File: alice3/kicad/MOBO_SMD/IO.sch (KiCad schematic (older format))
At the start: 36 parts, among them CON1 MicroSD, P2 USB_OTG, P3 UART1, SW2 SOFT RESET, U5 STM32F415RG, X1 MINI_DIN_6, Y2 16MHz

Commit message: Assign parts to footprints.
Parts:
- F1: footprint (none) -> Resistors_SMD:R_1210
- R22, R23, R24, R25: footprint (none) -> Resistors_SMD:R_0805
- X1: footprint mini_din-M_DIN6 -> cui-md-xxs:cui-md-60s
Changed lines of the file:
@@
 $EndDescr
 $Comp
-L +3.3V #PWR32
+L +3.3V #PWR014
 U 1 1 5689970E
 P 5750 950
-F 0 "#PWR32" H 5750 800 50  0001 C CNN
+F 0 "#PWR014" H 5750 800 50  0001 C CNN
 F 1 "+3.3V" H 5750 1090 50  0000 C CNN
 F 2 "" H 5750 950 60  0000 C CNN
@@
 NoConn ~ 8050 4700
 $Comp
-L GND #PWR35
+L GND #PWR015
 U 1 1 56899C9B
 P 7150 5900
-F 0 "#PWR35" H 7150 5650 50  0001 C CNN
+F 0 "#PWR015" H 7150 5650 50  0001 C CNN
 F 1 "GND" H 7150 5750 50  0000 C CNN
 F 2 "" H 7150 5900 60  0000 C CNN
@@
 $EndComp
 $Comp
-L +3.3V #PWR34
+L +3.3V #PWR016
 U 1 1 56899CD4
 P 7050 4050
-F 0 "#PWR34" H 7050 3900 50  0001 C CNN
+F 0 "#PWR016" H 7050 3900 50  0001 C CNN
 F 1 "+3.3V" H 7050 4190 50  0000 C CNN
 F 2 "" H 7050 4050 60  0000 C CNN
@@
 $EndComp
 $Comp
-L GND #PWR33
+L GND #PWR017
 U 1 1 568A1142
 P 5750 2250
-F 0 "#PWR33" H 5750 2000 50  0001 C CNN
+F 0 "#PWR017" H 5750 2000 50  0001 C CNN
 F 1 "GND" H 5750 2100 50  0000 C CNN
 F 2 "" H 5750 2250 60  0000 C CNN
@@
 NoConn ~ 8050 5400
 $Comp
-L PWR_FLAG #FLG1
+L PWR_FLAG #FLG018
 U 1 1 56A07E43
 P 8300 1300
-F 0 "#FLG1" H 8300 1395 50  0001 C CNN
+F 0 "#FLG018" H 8300 1395 50  0001 C CNN
 F 1 "PWR_FLAG" H 8300 1480 50  0000 C CNN
 F 2 "" H 8300 1300 50  0000 C CNN
@@
 $EndComp
 $Comp
-L +5V #PWR38
+L +5V #PWR019
 U 1 1 56A07E73
 P 8300 1600
-F 0 "#PWR38" H 8300 1450 50  0001 C CNN
+F 0 "#PWR019" H 8300 1450 50  0001 C CNN
 F 1 "+5V" H 8300 1740 50  0000 C CNN
 F 2 "" H 8300 1600 50  0000 C CNN
@@
 $EndComp
 $Comp
-L PWR_FLAG #FLG2
+L PWR_FLAG #FLG020
 U 1 1 56A0800D
 P 8900 1300
-F 0 "#FLG2" H 8900 1395 50  0001 C CNN
+F 0 "#FLG020" H 8900 1395 50  0001 C CNN
 F 1 "PWR_FLAG" H 8900 1480 50  0000 C CNN
 F 2 "" H 8900 1300 50  0000 C CNN
@@
 $EndComp
 $Comp
-L GND #PWR39
+L GND #PWR021
 U 1 1 56A08038
 P 8900 1600
-F 0 "#PWR39" H 8900 1350 50  0001 C CNN
+F 0 "#PWR021" H 8900 1350 50  0001 C CNN
 F 1 "GND" H 8900 1450 50  0000 C CNN
 F 2 "" H 8900 1600 50  0000 C CNN
@@
 $EndComp
 $Comp
-L GND #PWR37
+L GND #PWR022
 U 1 1 56A0883B
 P 7950 3100
-F 0 "#PWR37" H 7950 2850 50  0001 C CNN
+F 0 "#PWR022" H 7950 2850 50  0001 C CNN
 F 1 "GND" H 7950 2950 50  0000 C CNN
 F 2 "" H 7950 3100 50  0000 C CNN
@@
 $EndComp
 $Comp
-L +3.3V #PWR36
+L +3.3V #PWR023
 U 1 1 56A08841
 P 7500 2350
-F 0 "#PWR36" H 7500 2200 50  0001 C CNN
+F 0 "#PWR023" H 7500 2200 50  0001 C CNN
 F 1 "+3.3V" H 7500 2490 50  0000 C CNN
 F 2 "" H 7500 2350 50  0000 C CNN
@@
 A0
 $Comp
-L GND #PWR22
+L GND #PWR024
 U 1 1 56B85293
 P 1700 2800
-F 0 "#PWR22" H 1700 2550 50  0001 C CNN
+F 0 "#PWR024" H 1700 2550 50  0001 C CNN
 F 1 "GND" H 1700 2650 50  0000 C CNN
 F 2 "" H 1700 2800 60  0000 C CNN
@@
 $EndComp
 $Comp
-L +3.3V #PWR27
+L +3.3V #PWR025
 U 1 1 56BA49D2
 P 2300 1300
-F 0 "#PWR27" H 2300 1150 50  0001 C CNN
+F 0 "#PWR025" H 2300 1150 50  0001 C CNN
 F 1 "+3.3V" H 2300 1440 50  0000 C CNN
 F 2 "" H 2300 1300 60  0000 C CNN
@@
 $EndComp
 $Comp
-L GND #PWR23
+L GND #PWR026
 U 1 1 56BA4C6B
 P 1800 1400
-F 0 "#PWR23" H 1800 1150 50  0001 C CNN
+F 0 "#PWR026" H 1800 1150 50  0001 C CNN
 F 1 "GND" H 1800 1250 50  0000 C CNN
 F 2 "" H 1800 1400 60  0000 C CNN
@@
 $EndComp
 $Comp
-L GND #PWR31
+L GND #PWR027
 U 1 1 56BA634D
 P 4800 1450
-F 0 "#PWR31" H 4800 1200 50  0001 C CNN
+F 0 "#PWR027" H 4800 1200 50  0001 C CNN
 F 1 "GND" H 4800 1300 50  0000 C CNN
 F 2 "" H 4800 1450 60  0000 C CNN
@@
 $EndComp
 $Comp
-L +3.3V #PWR15
+L +3.3V #PWR028
 U 1 1 56BA6501
 P 900 2600
-F 0 "#PWR15" H 900 2450 50  0001 C CNN
+F 0 "#PWR028" H 900 2450 50  0001 C CNN
 F 1 "+3.3V" H 900 2740 50  0000 C CNN
 F 2 "" H 900 2600 60  0000 C CNN
@@
 $EndComp
 $Comp
-L GND #PWR16
+L GND #PWR029
 U 1 1 56BA66E5
 P 900 3450
-F 0 "#PWR16" H 900 3200 50  0001 C CNN
+F 0 "#PWR029" H 900 3200 50  0001 C CNN
 F 1 "GND" H 900 3300 50  0000 C CNN
 F 2 "" H 900 3450 60  0000 C CNN
@@
 $EndComp
 $Comp
-L +3.3V #PWR17
+L +3.3V #PWR030
 U 1 1 56BA9EA1
 P 1000 1900
-F 0 "#PWR17" H 1000 1750 50  0001 C CNN
+F 0 "#PWR030" H 1000 1750 50  0001 C CNN
 F 1 "+3.3V" H 1000 2040 50  0000 C CNN
 F 2 "" H 1000 1900 60  0000 C CNN
@@
 $EndComp
 $Comp
-L GND #PWR21
+L GND #PWR031
 U 1 1 56BAAE8C
 P 1600 2500
-F 0 "#PWR21" H 1600 2250 50  0001 C CNN
+F 0 "#PWR031" H 1600 2250 50  0001 C CNN
 F 1 "GND" H 1600 2350 50  0000 C CNN
 F 2 "" H 1600 2500 60  0000 C CNN
@@
 $EndComp
 $Comp
-L GND #PWR20
+L GND #PWR032
 U 1 1 56BAAEE8
 P 1450 2400
-F 0 "#PWR20" H 1450 2150 50  0001 C CNN
+F 0 "#PWR032" H 1450 2150 50  0001 C CNN
 F 1 "GND" H 1450 2250 50  0000 C CNN
 F 2 "" H 1450 2400 60  0000 C CNN
@@
 $EndComp
 $Comp
-L GND #PWR19
+L GND #PWR033
 U 1 1 56BAAF44
 P 1300 2300
-F 0 "#PWR19" H 1300 2050 50  0001 C CNN
+F 0 "#PWR033" H 1300 2050 50  0001 C CNN
 F 1 "GND" H 1300 2150 50  0000 C CNN
 F 2 "" H 1300 2300 60  0000 C CNN
@@
 $EndComp
 $Comp
-L GND #PWR18
+L GND #PWR034
 U 1 1 56BAAFA0
 P 1150 2200
-F 0 "#PWR18" H 1150 1950 50  0001 C CNN
+F 0 "#PWR034" H 1150 1950 50  0001 C CNN
 F 1 "GND" H 1150 2050 50  0000 C CNN
 F 2 "" H 1150 2200 60  0000 C CNN
@@
 $EndComp
 $Comp
-L GND #PWR14
+L GND #PWR035
 U 1 1 56BAAFFC
 P 800 2150
-F 0 "#PWR14" H 800 1900 50  0001 C CNN
+F 0 "#PWR035" H 800 1900 50  0001 C CNN
 F 1 "GND" H 800 2000 50  0000 C CNN
 F 2 "" H 800 2150 60  0000 C CNN
@@
 USB_D_P
 $Comp
-L GND #PWR24
+L GND #PWR036
 U 1 1 56BAB684
 P 1800 5850
-F 0 "#PWR24" H 1800 5600 50  0001 C CNN
+F 0 "#PWR036" H 1800 5600 50  0001 C CNN
 F 1 "GND" H 1800 5700 50  0000 C CNN
 F 2 "" H 1800 5850 60  0000 C CNN
@@
 $EndComp
 $Comp
-L +5V #PWR26
+L +5V #PWR037
 U 1 1 56BABB53
 P 2150 6990
-F 0 "#PWR26" H 2150 6840 50  0001 C CNN
+F 0 "#PWR037" H 2150 6840 50  0001 C CNN
 F 1 "+5V" H 2150 7130 50  0000 C CNN
 F 2 "" H 2150 6990 60  0000 C CNN
@@
 $EndComp
 $Comp
-L GND #PWR25
+L GND #PWR038
 U 1 1 56BAC7E3
 P 1850 7260
-F 0 "#PWR25" H 1850 7010 50  0001 C CNN
+F 0 "#PWR038" H 1850 7010 50  0001 C CNN
 F 1 "GND" H 1850 7110 50  0000 C CNN
 F 2 "" H 1850 7260 60  0000 C CNN
@@
 F 0 "X1" H 3400 7075 50  0000 L BNN
 F 1 "MINI_DIN_6" H 3800 7075 50  0000 L BNN
-F 2 "mini_din-M_DIN6" H 3800 6700 50  0001 C CNN
+F 2 "cui-md-xxs:cui-md-60s" H 3800 6700 50  0001 C CNN
 F 3 "" H 3800 6550 60  0000 C CNN
 	1    3800 6550
@@
 	1850 7220 1850 7260
 $Comp
-L +5V #PWR28
+L +5V #PWR039
 U 1 1 56CE0CE0
 P 3125 6200
-F 0 "#PWR28" H 3125 6050 50  0001 C CNN
+F 0 "#PWR039" H 3125 6050 50  0001 C CNN
 F 1 "+5V" H 3125 6340 50  0000 C CNN
 F 2 "" H 3125 6200 60  0000 C CNN
@@
 F 0 "R24" V 5130 6350 50  0000 C CNN
 F 1 "100" V 5050 6350 50  0000 C CNN
-F 2 "" V 4980 6350 30  0000 C CNN
+F 2 "Resistors_SMD:R_0805" V 4980 6350 30  0001 C CNN
 F 3 "" H 5050 6350 30  0000 C CNN
 	1    5050 6350
@@
 F 0 "R25" V 5130 6650 50  0000 C CNN
 F 1 "100" V 5050 6650 50  0000 C CNN
-F 2 "" V 4980 6650 30  0000 C CNN
+F 2 "Resistors_SMD:R_0805" V 4980 6650 30  0001 C CNN
 F 3 "" H 5050 6650 30  0000 C CNN
 	1    5050 6650
@@
 F 0 "R23" V 4880 6150 50  0000 C CNN
 F 1 "10K" V 4800 6150 50  0000 C CNN
-F 2 "" V 4730 6150 30  0000 C CNN
+F 2 "Resistors_SMD:R_0805" V 4730 6150 30  0001 C CNN
 F 3 "" H 4800 6150 30  0000 C CNN
 	1    4800 6150
@@
 F 0 "R22" V 4655 6150 50  0000 C CNN
 F 1 "10K" V 4575 6150 50  0000 C CNN
-F 2 "" V 4505 6150 30  0000 C CNN
+F 2 "Resistors_SMD:R_0805" V 4505 6150 30  0001 C CNN
 F 3 "" H 4575 6150 30  0000 C CNN
 	1    4575 6150
@@
 Connection ~ 4575 6650
 $Comp
-L +5V #PWR30
+L +5V #PWR040
 U 1 1 56CE2231
 P 4575 5900
-F 0 "#PWR30" H 4575 5750 50  0001 C CNN
+F 0 "#PWR040" H 4575 5750 50  0001 C CNN
 F 1 "+5V" H 4575 6040 50  0000 C CNN
 F 2 "" H 4575 5900 60  0000 C CNN
@@
 Connection ~ 4575 5950
 $Comp
-L GND #PWR29
+L GND #PWR041
 U 1 1 56CE2415
 P 4500 6825
-F 0 "#PWR29" H 4500 6575 50  0001 C CNN
+F 0 "#PWR041" H 4500 6575 50  0001 C CNN
 F 1 "GND" H 4500 6675 50  0000 C CNN
 F 2 "" H 4500 6825 60  0000 C CNN
@@
 F 0 "F1" H 1610 6610 50  0000 L CNN
 F 1 "F_Small" H 1530 6490 50  0000 L CNN
-F 2 "" H 1650 6550 50  0000 C CNN
+F 2 "Resistors_SMD:R_1210" H 1650 6550 50  0001 C CNN
 F 3 "" H 1650 6550 50  0000 C CNN
 	1    1650 6550

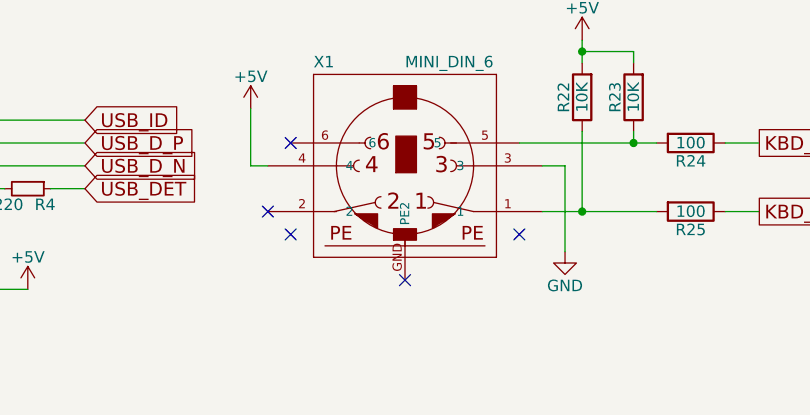
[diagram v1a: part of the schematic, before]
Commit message: Fix DIN pin numbers.
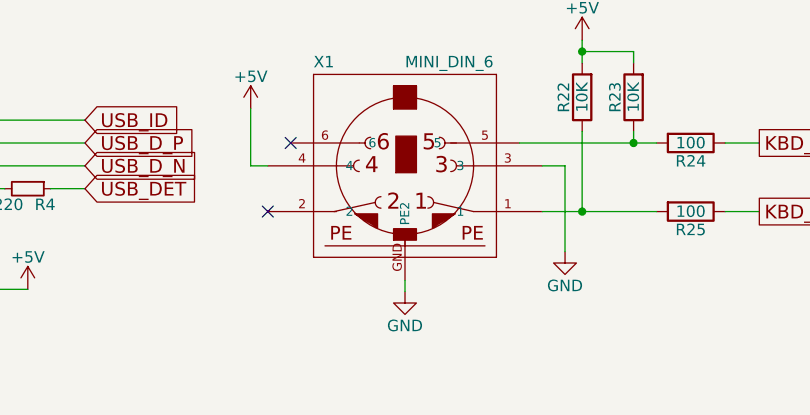
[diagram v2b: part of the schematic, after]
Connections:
- wire segments 103 -> 104
- no-connect marks 7 -> 4
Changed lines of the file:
@@
 NoConn ~ 3300 6350
 NoConn ~ 3200 6650
-NoConn ~ 3300 6750
-NoConn ~ 4300 6750
 Wire Wire Line
 	7150 4900 7150 5900
@@
 Text GLabel 3900 4700 2    60   BiDi ~ 0
 A17
-NoConn ~ 3800 6950
 Connection ~ 800  1900
+$Comp
+L GND #PWR?
+U 1 1 56D3ADAD
+P 3800 7000
+F 0 "#PWR?" H 3800 6750 50  0001 C CNN
+F 1 "GND" H 3800 6850 50  0000 C CNN
+F 2 "" H 3800 7000 50  0000 C CNN
+F 3 "" H 3800 7000 50  0000 C CNN
+	1    3800 7000
+	1    0    0    -1
+$EndComp
+Wire Wire Line
+	3800 6950 3800 7000
 $EndSCHEMATC

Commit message: Fix some footprint assignments.
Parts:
- C14: footprint Capacitors_ThroughHole:C_Radial_D5_L11_P2.5 -> Capacitors_SMD:C_1206
- C22: footprint Capacitors_SMD:C_0805 -> Capacitors_SMD:C_1206
- SW2: footprint Buttons_Switches_ThroughHole:SW_PUSH_SMALL -> Buttons_Switches_SMD:SW_SPST_PTS645
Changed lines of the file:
@@
 F 0 "C14" H 7375 5900 50  0000 L CNN
 F 1 "10µF" H 7375 5700 50  0000 L CNN
-F 2 "Capacitors_ThroughHole:C_Radial_D5_L11_P2.5" H 7350 5800 60  0001 C CNN
+F 2 "Capacitors_SMD:C_1206" H 7350 5800 60  0001 C CNN
 F 3 "" H 7350 5800 60  0000 C CNN
 	1    7350 5800
@@
 F 0 "SW2" H 5900 1460 50  0000 C CNN
 F 1 "SOFT RESET" H 5750 1270 50  0000 C CNN
-F 2 "Buttons_Switches_ThroughHole:SW_PUSH_SMALL" H 5750 1350 50  0001 C CNN
+F 2 "Buttons_Switches_SMD:SW_SPST_PTS645" H 5750 1350 50  0001 C CNN
 F 3 "" H 5750 1350 50  0000 C CNN
 	1    5750 1350
@@
 F 0 "C22" V 1050 2150 50  0000 L CNN
 F 1 "4.7µ" V 1050 1850 50  0000 L CNN
-F 2 "Capacitors_SMD:C_0805" H 1000 2100 60  0001 C CNN
+F 2 "Capacitors_SMD:C_1206" H 1000 2100 60  0001 C CNN
 F 3 "" H 1000 2100 60  0000 C CNN
 	1    1000 2100
@@
 Connection ~ 800  1900
 $Comp
-L GND #PWR?
+L GND #PWR042
 U 1 1 56D3ADAD
 P 3800 7000
-F 0 "#PWR?" H 3800 6750 50  0001 C CNN
+F 0 "#PWR042" H 3800 6750 50  0001 C CNN
 F 1 "GND" H 3800 6850 50  0000 C CNN
 F 2 "" H 3800 7000 50  0000 C CNN

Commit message: Add debug LED to IO board.
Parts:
- added D1: DEBUG LED, LEDs:LED-0805, symbol LED
- added R1: 10k, Resistors_SMD:R_0805, symbol R
- added R12: 100, Resistors_SMD:R_0805, symbol R
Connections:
- wire segments 104 -> 111
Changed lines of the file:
@@
 L GND #PWR027
 U 1 1 56BA634D
-P 4800 1450
-F 0 "#PWR027" H 4800 1200 50  0001 C CNN
-F 1 "GND" H 4800 1300 50  0000 C CNN
-F 2 "" H 4800 1450 60  0000 C CNN
-F 3 "" H 4800 1450 60  0000 C CNN
-	1    4800 1450
+P 5150 1450
+F 0 "#PWR027" H 5150 1200 50  0001 C CNN
+F 1 "GND" H 5150 1300 50  0000 C CNN
+F 2 "" H 5150 1450 60  0000 C CNN
+F 3 "" H 5150 1450 60  0000 C CNN
+	1    5150 1450
 	1    0    0    -1
 $EndComp
@@
 	2400 2400 2150 2400
 Wire Wire Line
-	4800 1450 3900 1450
-Wire Wire Line
 	2400 3000 900  3000
 Wire Wire Line
@@
 Wire Wire Line
 	3800 6950 3800 7000
+$Comp
+L LED D1
+U 1 1 56D3C057
+P 5150 1200
+F 0 "D1" H 5150 1300 50  0000 C CNN
+F 1 "DEBUG LED" H 5150 1100 50  0000 C CNN
+F 2 "LEDs:LED-0805" H 5150 1200 50  0001 C CNN
+F 3 "" H 5150 1200 50  0000 C CNN
+	1    5150 1200
+	0    -1   -1   0
+$EndComp
+$Comp
+L R R1
+U 1 1 56D3C114
+P 4900 1050
+F 0 "R1" V 4980 1050 50  0000 C CNN
+F 1 "10k" V 4900 1050 50  0000 C CNN
+F 2 "Resistors_SMD:R_0805" V 4830 1050 30  0001 C CNN
+F 3 "" H 4900 1050 30  0000 C CNN
+	1    4900 1050
+	1    0    0    -1
+$EndComp
+$Comp
+L R R12
+U 1 1 56D3C19F
+P 5150 800
+F 0 "R12" V 5230 800 50  0000 C CNN
+F 1 "100" V 5150 800 50  0000 C CNN
+F 2 "Resistors_SMD:R_0805" V 5080 800 30  0001 C CNN
+F 3 "" H 5150 800 30  0000 C CNN
+	1    5150 800
+	1    0    0    -1
+$EndComp
+Wire Wire Line
+	3900 1450 4700 1450
+Wire Wire Line
+	4700 1450 4700 650
+Wire Wire Line
+	4700 650  5150 650
+Wire Wire Line
+	4900 650  4900 900
+Connection ~ 4900 650
+Wire Wire Line
+	4900 1200 4900 1450
+Wire Wire Line
+	4900 1450 5150 1450
+Wire Wire Line
+	5150 1450 5150 1400
+Wire Wire Line
+	5150 1000 5150 950
 $EndSCHEMATC

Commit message: Remove R5 pull-down resistor for soft reset button.
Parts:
- removed R5: 10k, Resistors_SMD:R_0805, symbol R
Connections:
- wire segments 111 -> 110
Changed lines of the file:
@@
 CS
-$Comp
-L R R5
-U 1 1 568A0A99
-P 5750 2000
-F 0 "R5" V 5830 2000 50  0000 C CNN
-F 1 "10k" V 5750 2000 50  0000 C CNN
-F 2 "Resistors_SMD:R_0805" V 5680 2000 30  0001 C CNN
-F 3 "" H 5750 2000 30  0000 C CNN
-	1    5750 2000
-	1    0    0    -1
-$EndComp
-$Comp
-L GND #PWR017
-U 1 1 568A1142
-P 5750 2250
-F 0 "#PWR017" H 5750 2000 50  0001 C CNN
-F 1 "GND" H 5750 2100 50  0000 C CNN
-F 2 "" H 5750 2250 60  0000 C CNN
-F 3 "" H 5750 2250 60  0000 C CNN
-	1    5750 2250
-	1    0    0    -1
-$EndComp
 $Comp
 L CP1 C14
@@
 	5750 950  5750 1050
 Wire Wire Line
-	5750 1650 5750 1850
-Wire Wire Line
-	5750 2150 5750 2250
-Connection ~ 5750 1750
-Wire Wire Line
 	8300 1300 8300 1600
 Wire Wire Line
@@
 Wire Wire Line
 	5150 1000 5150 950
+Wire Wire Line
+	5750 1650 5750 1750
 $EndSCHEMATC

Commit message: More routing.
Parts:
- CON1: footprint microsd:microsd_socket -> Molex:microsd_1040310811
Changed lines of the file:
@@
 F 0 "CON1" H 8300 5500 50  0000 C CNN
 F 1 "MicroSD" H 9200 4550 50  0000 C CNN
-F 2 "microsd:microsd_socket" H 9150 5300 50  0001 C CNN
+F 2 "Molex:microsd_1040310811" H 9150 5300 50  0001 C CNN
 F 3 "" H 8950 4950 50  0000 C CNN
 	1    8750 5050

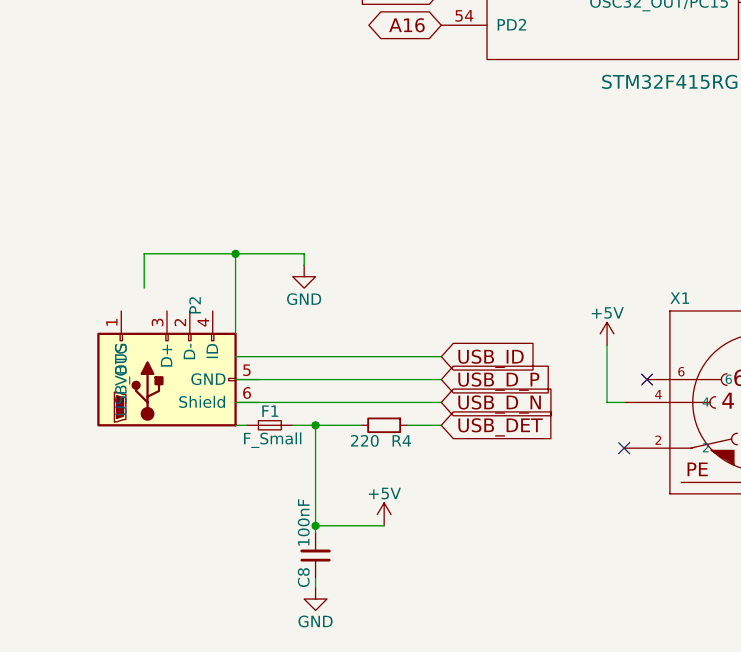
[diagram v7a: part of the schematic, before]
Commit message: update microUSB schematic part
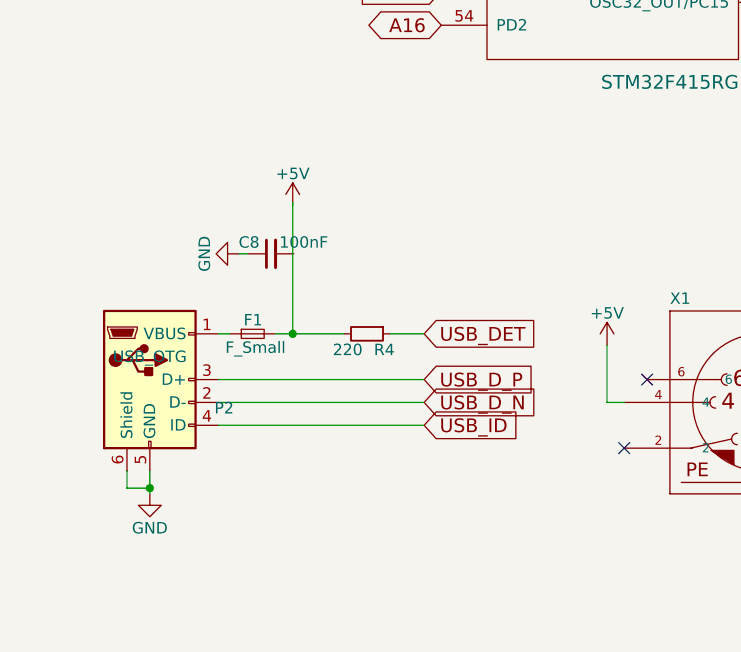
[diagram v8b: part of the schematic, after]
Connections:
- wire segments 110 -> 108
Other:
- moved on the sheet: C8, F1, P2, R4
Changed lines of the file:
@@
 L USB_OTG P2
 U 1 1 56BAA76F
-P 1200 6350
-F 0 "P2" H 1525 6225 50  0000 C CNN
-F 1 "USB_OTG" H 1200 6550 50  0000 C CNN
-F 2 "microusb:10118192-0001LF" V 1150 6250 60  0001 C CNN
-F 3 "" V 1150 6250 60  0000 C CNN
-	1    1200 6350
-	0    -1   -1   0
+P 1125 6350
+F 0 "P2" H 1450 6225 50  0000 C CNN
+F 1 "USB_OTG" H 1125 6450 50  0000 C CNN
+F 2 "microusb:10118192-0001LF" V 1075 6250 60  0001 C CNN
+F 3 "" V 1075 6250 60  0000 C CNN
+	1    1125 6350
+	1    0    0    -1
 $EndComp
 $Comp
@@
 Text GLabel 2400 4350 0    60   Input ~ 0
 USB_D_P
-Text GLabel 2400 6550 2    60   Input ~ 0
+Text GLabel 2325 6150 2    60   Input ~ 0
 USB_DET
-Text GLabel 2400 6250 2    60   Input ~ 0
+Text GLabel 2325 6550 2    60   Input ~ 0
 USB_ID
-Text GLabel 2400 6450 2    60   Input ~ 0
+Text GLabel 2325 6450 2    60   Input ~ 0
 USB_D_N
-Text GLabel 2400 6350 2    60   Input ~ 0
+Text GLabel 2325 6350 2    60   Input ~ 0
 USB_D_P
 $Comp
 L GND #PWR035
 U 1 1 56BAB684
-P 1800 5850
-F 0 "#PWR035" H 1800 5600 50  0001 C CNN
-F 1 "GND" H 1800 5700 50  0000 C CNN
-F 2 "" H 1800 5850 60  0000 C CNN
-F 3 "" H 1800 5850 60  0000 C CNN
-	1    1800 5850
+P 1125 6850
+F 0 "#PWR035" H 1125 6600 50  0001 C CNN
+F 1 "GND" H 1125 6700 50  0000 C CNN
+F 2 "" H 1125 6850 60  0000 C CNN
+F 3 "" H 1125 6850 60  0000 C CNN
+	1    1125 6850
 	1    0    0    -1
 $EndComp
@@
 L +5V #PWR036
 U 1 1 56BABB53
-P 2150 6990
-F 0 "#PWR036" H 2150 6840 50  0001 C CNN
-F 1 "+5V" H 2150 7130 50  0000 C CNN
-F 2 "" H 2150 6990 60  0000 C CNN
-F 3 "" H 2150 6990 60  0000 C CNN
-	1    2150 6990
+P 1750 5590
+F 0 "#PWR036" H 1750 5440 50  0001 C CNN
+F 1 "+5V" H 1750 5730 50  0000 C CNN
+F 2 "" H 1750 5590 60  0000 C CNN
+F 3 "" H 1750 5590 60  0000 C CNN
+	1    1750 5590
 	1    0    0    -1
 $EndComp
@@
 L R_Small R4
 U 1 1 56BAC147
-P 2150 6550
-F 0 "R4" V 2220 6580 50  0000 L CNN
-F 1 "220" V 2220 6400 50  0000 L CNN
-F 2 "Resistors_SMD:R_0805" H 2150 6550 60  0001 C CNN
-F 3 "" H 2150 6550 60  0000 C CNN
-	1    2150 6550
+P 2075 6150
+F 0 "R4" V 2145 6180 50  0000 L CNN
+F 1 "220" V 2145 6000 50  0000 L CNN
+F 2 "Resistors_SMD:R_0805" H 2075 6150 60  0001 C CNN
+F 3 "" H 2075 6150 60  0000 C CNN
+	1    2075 6150
 	0    1    1    0
 $EndComp
@@
 L GND #PWR037
 U 1 1 56BAC7E3
-P 1850 7260
-F 0 "#PWR037" H 1850 7010 50  0001 C CNN
-F 1 "GND" H 1850 7110 50  0000 C CNN
-F 2 "" H 1850 7260 60  0000 C CNN
-F 3 "" H 1850 7260 60  0000 C CNN
-	1    1850 7260
-	1    0    0    -1
+P 1515 5800
+F 0 "#PWR037" H 1515 5550 50  0001 C CNN
+F 1 "GND" H 1515 5650 50  0000 C CNN
+F 2 "" H 1515 5800 60  0000 C CNN
+F 3 "" H 1515 5800 60  0000 C CNN
+	1    1515 5800
+	0    1    1    0
 $EndComp
 $Comp
 L C_Small C8
 U 1 1 56BAC974
-P 1850 7120
-F 0 "C8" V 1900 7170 50  0000 L CNN
-F 1 "100nF" V 1900 6870 50  0000 L CNN
-F 2 "Capacitors_SMD:C_0805" H 1850 7120 60  0001 C CNN
-F 3 "" H 1850 7120 60  0000 C CNN
-	1    1850 7120
-	-1   0    0    1
+P 1655 5800
+F 0 "C8" V 1705 5850 50  0000 L CNN
+F 1 "100nF" V 1705 5550 50  0000 L CNN
+F 2 "Capacitors_SMD:C_0805" H 1655 5800 60  0001 C CNN
+F 3 "" H 1655 5800 60  0000 C CNN
+	1    1655 5800
+	0    -1   -1   0
 $EndComp
 Text GLabel 3900 4500 2    60   BiDi ~ 0
@@
 	3900 1950 4300 1950
 Wire Wire Line
-	1500 6150 1500 5800
-Wire Wire Line
-	1100 5800 1800 5800
-Wire Wire Line
-	1100 5950 1100 5800
-Connection ~ 1500 5800
-Wire Wire Line
-	1500 6250 2400 6250
-Wire Wire Line
-	1500 6350 2400 6350
-Wire Wire Line
-	1500 6450 2400 6450
-Wire Wire Line
-	1850 6550 1850 7020
-Wire Wire Line
-	1850 6990 2150 6990
-Wire Wire Line
-	1800 5800 1800 5850
-Wire Wire Line
-	2250 6550 2400 6550
-Connection ~ 1850 6990
-Wire Wire Line
-	1850 7220 1850 7260
+	1425 6550 2325 6550
+Wire Wire Line
+	1425 6350 2325 6350
+Wire Wire Line
+	1425 6450 2325 6450
+Wire Wire Line
+	2175 6150 2325 6150
+Wire Wire Line
+	1555 5800 1515 5800
 $Comp
 L +5V #PWR038
@@
 L F_Small F1
 U 1 1 56D390B2
-P 1650 6550
-F 0 "F1" H 1610 6610 50  0000 L CNN
-F 1 "F_Small" H 1530 6490 50  0000 L CNN
-F 2 "Resistors_SMD:R_1210" H 1650 6550 50  0001 C CNN
-F 3 "" H 1650 6550 50  0000 C CNN
-	1    1650 6550
-	1    0    0    -1
-$EndComp
-Wire Wire Line
-	1500 6550 1550 6550
-Wire Wire Line
-	1750 6550 2050 6550
-Connection ~ 1850 6550
+P 1575 6150
+F 0 "F1" H 1535 6210 50  0000 L CNN
+F 1 "F_Small" H 1455 6090 50  0000 L CNN
+F 2 "Resistors_SMD:R_1210" H 1575 6150 50  0001 C CNN
+F 3 "" H 1575 6150 50  0000 C CNN
+	1    1575 6150
+	1    0    0    -1
+$EndComp
+Wire Wire Line
+	1425 6150 1475 6150
+Wire Wire Line
+	1675 6150 1975 6150
 Text GLabel 3900 4600 2    60   Input ~ 0
 ~PROP_READY~
@@
 Wire Wire Line
 	5750 1650 5750 1750
+Wire Wire Line
+	1125 6850 1125 6750
+Wire Wire Line
+	1025 6750 1025 6825
+Wire Wire Line
+	1025 6825 1125 6825
+Connection ~ 1125 6825
+Wire Wire Line
+	1750 5575 1750 6150
+Connection ~ 1750 6150
 $EndSCHEMATC
